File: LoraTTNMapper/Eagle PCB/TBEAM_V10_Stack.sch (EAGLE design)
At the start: 13 parts, among them IC2 ULN2003AD, U1 GY-521MPU6050

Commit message: Gyro + PCB
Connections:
- net N$1: now also U$1.GPIO04; no longer U$1.GPIO00
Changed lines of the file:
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@@
-</segment>
-</net>
-<net name="N$1" class="0">
-<segment>
-<pinref part="U1" gate="G$1" pin="INT"/>
-<pinref part="U$1" gate="G$1" pin="GPIO00"/>
-<wire x1="104.14" y1="88.9" x2="58.42" y2="88.9" width="0.1524" layer="91"/>
-<wire x1="58.42" y1="88.9" x2="58.42" y2="73.66" width="0.1524" layer="91"/>
 </segment>
 </net>
@@
 </segment>
 </net>
+<net name="N$1" class="0">
+<segment>
+<pinref part="U1" gate="G$1" pin="INT"/>
+<pinref part="U$1" gate="G$1" pin="GPIO04"/>
+<wire x1="104.14" y1="88.9" x2="55.88" y2="88.9" width="0.1524" layer="91"/>
+<wire x1="55.88" y1="88.9" x2="55.88" y2="73.66" width="0.1524" layer="91"/>
+</segment>
+</net>

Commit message: So long so good
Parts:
- added C1, C2: 100nF, rcl:C-US050-024X044
- added D1, D2, D3, D4, D5, D6, D7, D8: (no value), diode:DIODE-D-5
- added IC1: L298, st-microelectronics:L298
- added J1, J2, J3: 1X2-3.5MM, adafruit:1X2-3.5MM
- renumbered JP2 to SERVO_2
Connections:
- new net N$10: D5.A, D7.C, IC1.OUT3, J3.1
- new net N$7: D1.A, D2.C, IC1.OUT1, J2.1
- new net N$8: D3.A, D4.C, IC1.OUT2, J2.2
- new net N$9: D6.A, D8.C, IC1.OUT4, J3.2
- new net V+: C2.1, D1.C, D3.C, D5.C, D6.C, IC1.VS, J1.1
- net +5V: now also C1.1, IC1.VCC
- net GND: now also C1.2, C2.2, D2.A, D4.A, D7.A, D8.A, IC1.GND, IC1.SEN_A, IC1.SEN_B, J1.2
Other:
- note added: "GPIO 4 = Gyro Interrupt"
- note added: "Todo: Servo 2 an Power Rail"
- note removed: "GPIO 0 = Gyro Interrupt"

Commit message: Board Layout
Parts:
- removed U1: GY-521MPU6050, gy-521:GY-521MPU6050
- LED1: value (none) -> Power Rail
- renumbered SERVO_2 to SERVO_2/GPIO32
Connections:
- removed net N$1: U$1.GPIO04, U1.INT
- net GND: no longer U1.GND
- net SCL: no longer U1.SCL
- net SDA: no longer U1.SDA
- net VDD: no longer U1.VCC
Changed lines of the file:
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@@
 <?xml version="1.0" encoding="utf-8"?>
 <!DOCTYPE eagle SYSTEM "eagle.dtd">
-<eagle version="9.5.2">
+<eagle version="9.6.2">
 <drawing>
 <settings>
@@
 <part name="IC2" library="uln-udn" deviceset="ULN2003A" device="D"/>
 <part name="SERVO_1" library="pinhead" deviceset="PINHD-1X3" device=""/>
-<part name="SERVO_2" library="pinhead" deviceset="PINHD-1X3" device="" value="Servo_2"/>
-<part name="LED1" library="led" deviceset="LED" device="SML1206"/>
+<part name="SERVO_2/GPIO32" library="pinhead" deviceset="PINHD-1X3" device="" value="Servo_2"/>
+<part name="LED1" library="led" deviceset="LED" device="SML1206" value="Power Rail"/>
 <part name="R1" library="resistor" deviceset="R-EU_" device="R1206"/>
 <part name="R2" library="resistor" deviceset="R-EU_" device="R1206"/>
@@
 <part name="LED2" library="led" deviceset="LED" device="SML1206"/>
 <part name="LED3" library="led" deviceset="LED" device="SML1206"/>
-<part name="U1" library="gy-521" deviceset="GY-521" device="MPU6050"/>
 <part name="3V1" library="supply2" deviceset="VDD" device=""/>
 <part name="IC1" library="st-microelectronics" deviceset="L298" device=""/>
@@
 <attribute name="VALUE" x="260.35" y="68.58" size="1.778" layer="96" rot="R180"/>
 </instance>
-<instance part="SERVO_2" gate="A" x="254" y="40.64" smashed="yes" rot="R180">
+<instance part="SERVO_2/GPIO32" gate="A" x="254" y="40.64" smashed="yes" rot="R180">
 <attribute name="NAME" x="260.35" y="34.925" size="1.778" layer="95" rot="R180"/>
 <attribute name="VALUE" x="260.35" y="48.26" size="1.778" layer="96" rot="R180"/>
@@
 <attribute name="VALUE" x="153.035" y="20.828" size="1.778" layer="96" rot="R90"/>
 </instance>
-<instance part="U1" gate="G$1" x="119.38" y="109.22" smashed="yes"/>
 <instance part="3V1" gate="G$1" x="63.5" y="81.28" smashed="yes"/>
 <instance part="IC1" gate="L298" x="218.44" y="195.58" smashed="yes">
@@
 <junction x="205.74" y="35.56"/>
 <wire x1="248.92" y1="60.96" x2="256.54" y2="60.96" width="0.1524" layer="91"/>
-<pinref part="SERVO_2" gate="A" pin="2"/>
+<pinref part="SERVO_2/GPIO32" gate="A" pin="2"/>
 <wire x1="256.54" y1="40.64" x2="233.68" y2="40.64" width="0.1524" layer="91"/>
 <junction x="233.68" y="40.64"/>
@@
 <junction x="256.54" y="40.64"/>
 <label x="226.06" y="76.2" size="1.778" layer="95"/>
-</segment>
-<segment>
-<pinref part="U1" gate="G$1" pin="VCC"/>
-<wire x1="104.14" y1="124.46" x2="96.52" y2="124.46" width="0.1524" layer="91"/>
-<label x="96.52" y="124.46" size="1.778" layer="95"/>
 </segment>
 </net>
@@
 <junction x="142.24" y="20.32"/>
 <label x="139.7" y="17.78" size="1.778" layer="95"/>
-</segment>
-<segment>
-<pinref part="U1" gate="G$1" pin="GND"/>
-<wire x1="104.14" y1="119.38" x2="96.52" y2="119.38" width="0.1524" layer="91"/>
-<label x="93.98" y="119.38" size="1.778" layer="95"/>
 </segment>
 <segment>
@@
 <label x="152.4" y="68.58" size="1.778" layer="95"/>
 </segment>
-<segment>
-<pinref part="U1" gate="G$1" pin="SCL"/>
-<wire x1="104.14" y1="114.3" x2="96.52" y2="114.3" width="0.1524" layer="91"/>
-<label x="93.98" y="114.3" size="1.778" layer="95"/>
-</segment>
 </net>
 <net name="SDA" class="0">
@@
 <wire x1="167.64" y1="99.06" x2="182.88" y2="99.06" width="0.1524" layer="91"/>
 <label x="187.96" y="99.06" size="1.778" layer="95"/>
-</segment>
-<segment>
-<pinref part="U1" gate="G$1" pin="SDA"/>
-<wire x1="104.14" y1="109.22" x2="96.52" y2="109.22" width="0.1524" layer="91"/>
-<label x="93.98" y="109.22" size="1.778" layer="95"/>
 </segment>
 </net>
@@
 <wire x1="205.74" y1="58.42" x2="205.74" y2="53.34" width="0.1524" layer="91"/>
 <junction x="205.74" y="53.34"/>
-<pinref part="SERVO_2" gate="A" pin="1"/>
+<pinref part="SERVO_2/GPIO32" gate="A" pin="1"/>
 <wire x1="256.54" y1="38.1" x2="238.76" y2="38.1" width="0.1524" layer="91"/>
 <wire x1="238.76" y1="38.1" x2="238.76" y2="58.42" width="0.1524" layer="91"/>
@@
 <net name="GPIO32" class="0">
 <segment>
-<pinref part="SERVO_2" gate="A" pin="3"/>
+<pinref part="SERVO_2/GPIO32" gate="A" pin="3"/>
 <wire x1="256.54" y1="43.18" x2="243.84" y2="43.18" width="0.1524" layer="91"/>
 <label x="241.3" y="43.18" size="1.778" layer="95"/>
@@
 </segment>
 </net>
-<net name="N$1" class="0">
-<segment>
-<pinref part="U1" gate="G$1" pin="INT"/>
-<pinref part="U$1" gate="G$1" pin="GPIO04"/>
-<wire x1="104.14" y1="88.9" x2="55.88" y2="88.9" width="0.1524" layer="91"/>
-<wire x1="55.88" y1="88.9" x2="55.88" y2="73.66" width="0.1524" layer="91"/>
-</segment>
-</net>

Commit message: pcb layout
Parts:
- added INA219: (no value), pinhead:PINHD-1X6
- added SOLAR_IN: (no value), con-wago-500:W237-102
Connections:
- new net V_IN_+: INA219.1, SOLAR_IN-1.KL
- new net V_OUT_+: INA219.2
- net GND: now also INA219.5, SOLAR_IN-2.KL
- net SCL: now also INA219.4
- net SDA: now also INA219.3
- net VDD_SWITCHABLE: now also INA219.6
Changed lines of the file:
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@@
 <part name="GND8" library="supply1" deviceset="GND" device=""/>
 <part name="GND9" library="supply1" deviceset="GND" device=""/>
+<part name="INA219" library="pinhead" library_urn="urn:adsk.eagle:library:325" deviceset="PINHD-1X6" device="" package3d_urn="urn:adsk.eagle:package:22472/2"/>
+<part name="SOLAR_IN" library="con-wago-500" library_urn="urn:adsk.eagle:library:195" deviceset="W237-102" device="" package3d_urn="urn:adsk.eagle:package:10688/1"/>
+<part name="GND2" library="supply1" deviceset="GND" device=""/>
 </parts>
 <sheets>
@@
 <instance part="GND9" gate="1" x="236.22" y="167.64" smashed="yes">
 <attribute name="VALUE" x="233.68" y="165.1" size="1.778" layer="96"/>
+</instance>
+<instance part="INA219" gate="A" x="30.48" y="193.04" smashed="yes">
+<attribute name="NAME" x="24.13" y="203.835" size="1.778" layer="95"/>
+<attribute name="VALUE" x="24.13" y="182.88" size="1.778" layer="96"/>
+</instance>
+<instance part="SOLAR_IN" gate="-1" x="-20.32" y="203.2" smashed="yes">
+<attribute name="NAME" x="-20.32" y="204.089" size="1.778" layer="95" rot="R180"/>
+</instance>
+<instance part="SOLAR_IN" gate="-2" x="-20.32" y="198.12" smashed="yes">
+<attribute name="VALUE" x="-22.86" y="194.437" size="1.778" layer="96"/>
+<attribute name="NAME" x="-20.32" y="199.009" size="1.778" layer="95" rot="R180"/>
+</instance>
+<instance part="GND2" gate="1" x="-12.7" y="193.04" smashed="yes">
+<attribute name="VALUE" x="-15.24" y="190.5" size="1.778" layer="96"/>
 </instance>
 </instances>
@@
 <junction x="236.22" y="203.2"/>
 </segment>
+<segment>
+<pinref part="INA219" gate="A" pin="5"/>
+<junction x="27.94" y="190.5"/>
+<wire x1="27.94" y1="190.5" x2="43.18" y2="190.5" width="0.1524" layer="91"/>
+<label x="45.72" y="190.5" size="1.778" layer="95"/>
+</segment>
+<segment>
+<pinref part="SOLAR_IN" gate="-2" pin="KL"/>
+<pinref part="GND2" gate="1" pin="GND"/>
+<wire x1="-15.24" y1="198.12" x2="-12.7" y2="198.12" width="0.1524" layer="91"/>
+<wire x1="-12.7" y1="198.12" x2="-12.7" y2="195.58" width="0.1524" layer="91"/>
+<label x="-10.16" y="195.58" size="1.778" layer="95"/>
+</segment>
 </net>
 <net name="SCL" class="0">
@@
 <label x="152.4" y="68.58" size="1.778" layer="95"/>
 </segment>
+<segment>
+<wire x1="27.94" y1="193.04" x2="30.48" y2="193.04" width="0.1524" layer="91"/>
+<pinref part="INA219" gate="A" pin="4"/>
+<junction x="30.48" y="193.04"/>
+<wire x1="30.48" y1="193.04" x2="43.18" y2="193.04" width="0.1524" layer="91"/>
+<junction x="27.94" y="193.04"/>
+<label x="45.72" y="193.04" size="1.778" layer="95"/>
+</segment>
 </net>
 <net name="SDA" class="0">
@@
 <wire x1="167.64" y1="99.06" x2="182.88" y2="99.06" width="0.1524" layer="91"/>
 <label x="187.96" y="99.06" size="1.778" layer="95"/>
+</segment>
+<segment>
+<wire x1="27.94" y1="195.58" x2="30.48" y2="195.58" width="0.1524" layer="91"/>
+<pinref part="INA219" gate="A" pin="3"/>
+<label x="45.72" y="195.58" size="1.778" layer="95"/>
+<junction x="30.48" y="195.58"/>
+<wire x1="30.48" y1="195.58" x2="43.18" y2="195.58" width="0.1524" layer="91"/>
+<junction x="27.94" y="195.58"/>
 </segment>
 </net>
@@
 <wire x1="167.64" y1="91.44" x2="182.88" y2="91.44" width="0.1524" layer="91"/>
 <label x="187.96" y="91.44" size="1.778" layer="95"/>
+</segment>
+<segment>
+<pinref part="INA219" gate="A" pin="6"/>
+<junction x="27.94" y="187.96"/>
+<wire x1="27.94" y1="187.96" x2="43.18" y2="187.96" width="0.1524" layer="91"/>
+<label x="45.72" y="187.96" size="1.778" layer="95"/>
 </segment>
 </net>
@@
 </segment>
 </net>
+<net name="V_IN_+" class="0">
+<segment>
+<pinref part="SOLAR_IN" gate="-1" pin="KL"/>
+<pinref part="INA219" gate="A" pin="1"/>
+<wire x1="-15.24" y1="203.2" x2="27.94" y2="203.2" width="0.1524" layer="91"/>
+<wire x1="27.94" y1="203.2" x2="27.94" y2="200.66" width="0.1524" layer="91"/>
+<junction x="-15.24" y="203.2"/>
+<junction x="27.94" y="200.66"/>
+<label x="45.72" y="200.66" size="1.778" layer="95"/>
+<label x="-15.24" y="210.82" size="1.778" layer="95"/>
+</segment>
+</net>
+<net name="V_OUT_+" class="0">
+<segment>
+<pinref part="INA219" gate="A" pin="2"/>
+<wire x1="27.94" y1="198.12" x2="43.18" y2="198.12" width="0.1524" layer="91"/>
+<label x="45.72" y="198.12" size="1.778" layer="95"/>
+<junction x="27.94" y="198.12"/>
+</segment>
+</net>
+</nets>
+</sheet>
+<sheet>
+<plain>
+</plain>
+<instances>
+</instances>
+<busses>
+</busses>
+<nets>
 </nets>
 </sheet>
@@
 which will not be processed correctly with this version.
 </note>
+<note version="8.2" severity="warning">
+Since Version 8.2, EAGLE supports online libraries. The ids
+of those online libraries will not be understood (or retained)
+with this version.
+</note>
+<note version="8.3" severity="warning">
+Since Version 8.3, EAGLE supports URNs for individual library
+assets (packages, symbols, and devices). The URNs of those assets
+will not be understood (or retained) with this version.
+</note>
+<note version="8.3" severity="warning">
+Since Version 8.3, EAGLE supports the association of 3D packages
+with devices in libraries, schematics, and board files. Those 3D
+packages will not be understood (or retained) with this version.
+</note>
 </compatibility>

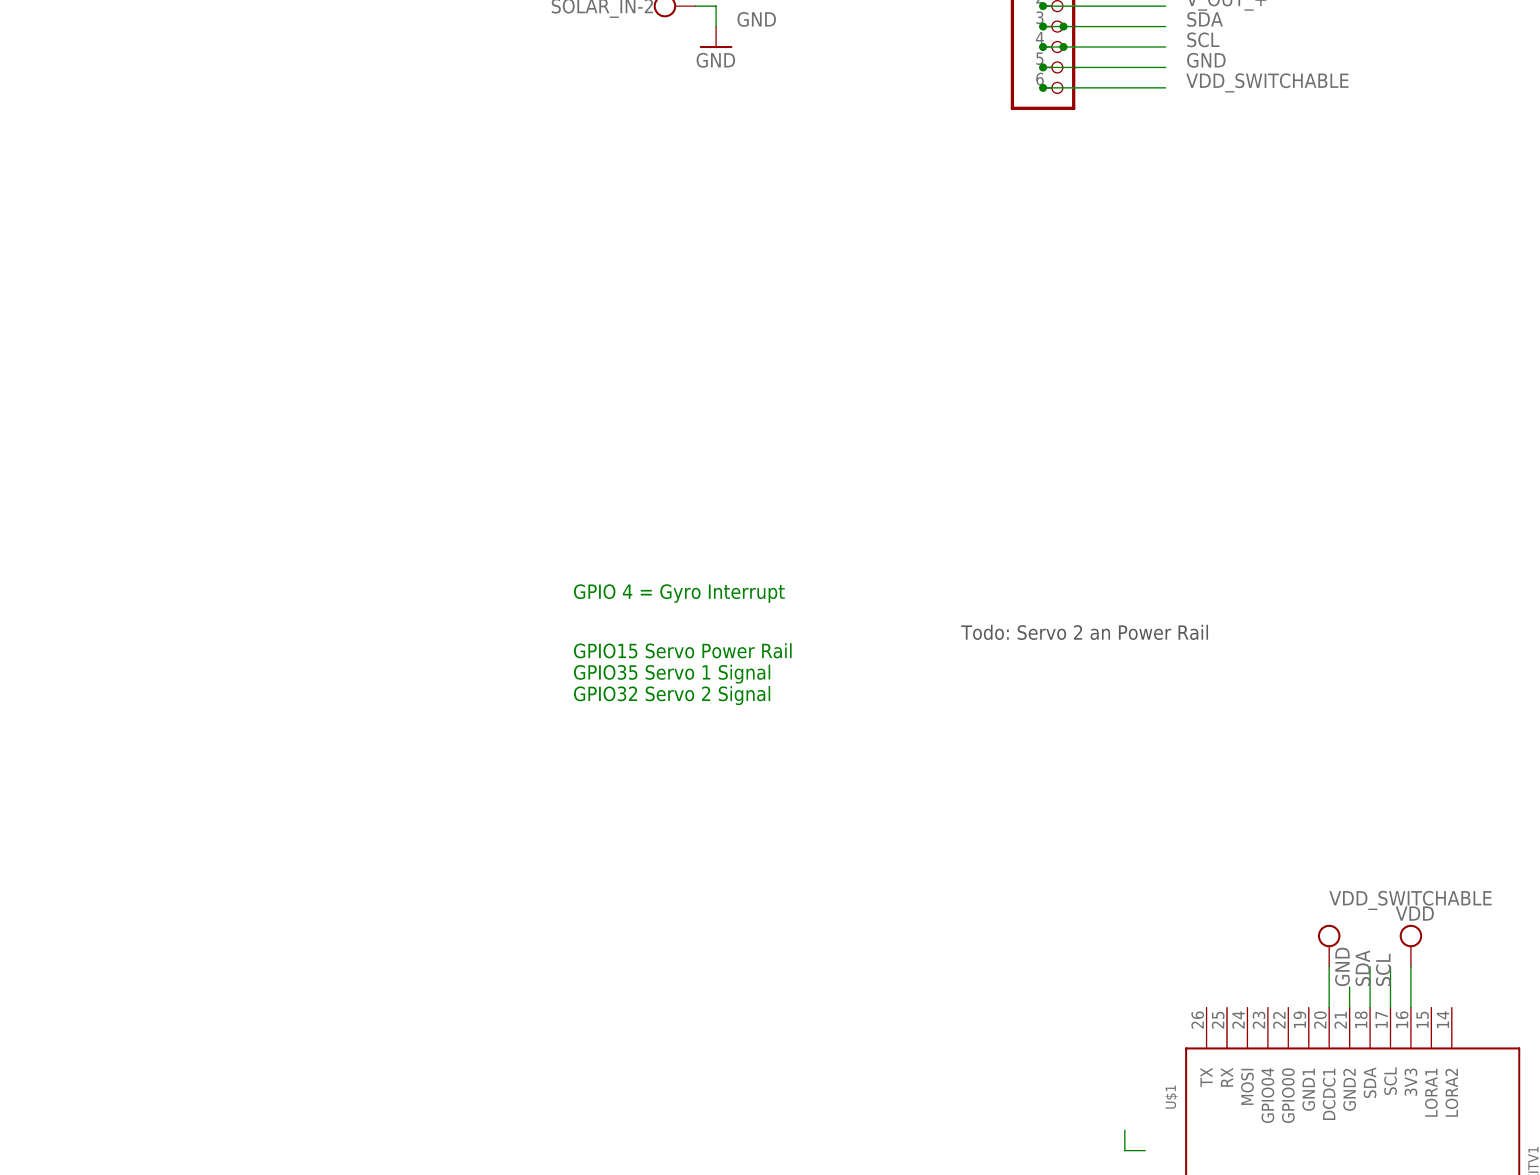
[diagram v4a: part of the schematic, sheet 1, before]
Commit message: PCB Update P Mosfet to switch Solar Panel
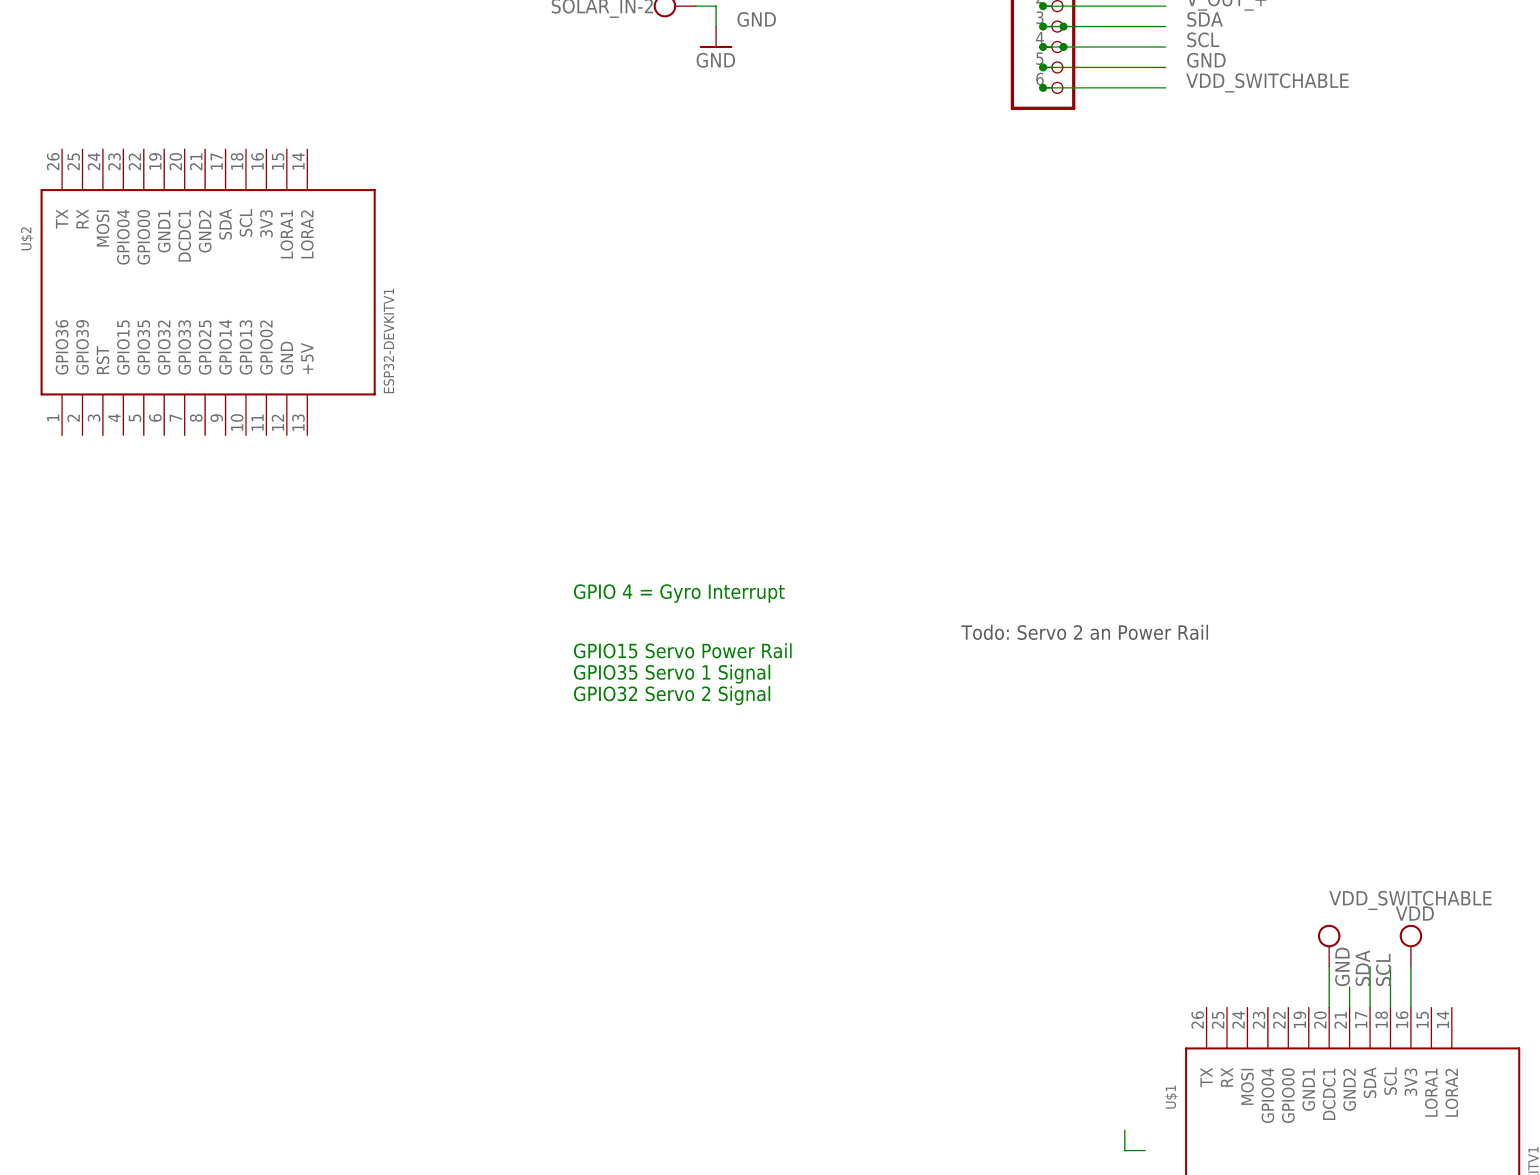
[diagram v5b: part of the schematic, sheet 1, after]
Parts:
- added U$2: ESP32DEVKITV1, TTGO T-Beam V10:ESP32DEVKITV1
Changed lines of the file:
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@@
 <part name="SOLAR_IN" library="con-wago-500" library_urn="urn:adsk.eagle:library:195" deviceset="W237-102" device="" package3d_urn="urn:adsk.eagle:package:10688/1"/>
 <part name="GND2" library="supply1" deviceset="GND" device=""/>
+<part name="U$2" library="TTGO T-Beam V10" deviceset="ESP32DEVKITV1" device=""/>
 </parts>
 <sheets>
@@
 <attribute name="VALUE" x="-15.24" y="190.5" size="1.778" layer="96"/>
 </instance>
+<instance part="U$2" gate="G$1" x="-71.12" y="162.56" smashed="yes">
+<attribute name="NAME" x="-97.79" y="167.64" size="1.27" layer="95" rot="R90"/>
+</instance>
 </instances>
